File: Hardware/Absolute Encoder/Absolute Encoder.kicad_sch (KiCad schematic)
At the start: 15 parts, among them J1 Conn_01x05, U1 74LS165, U2 74LS165

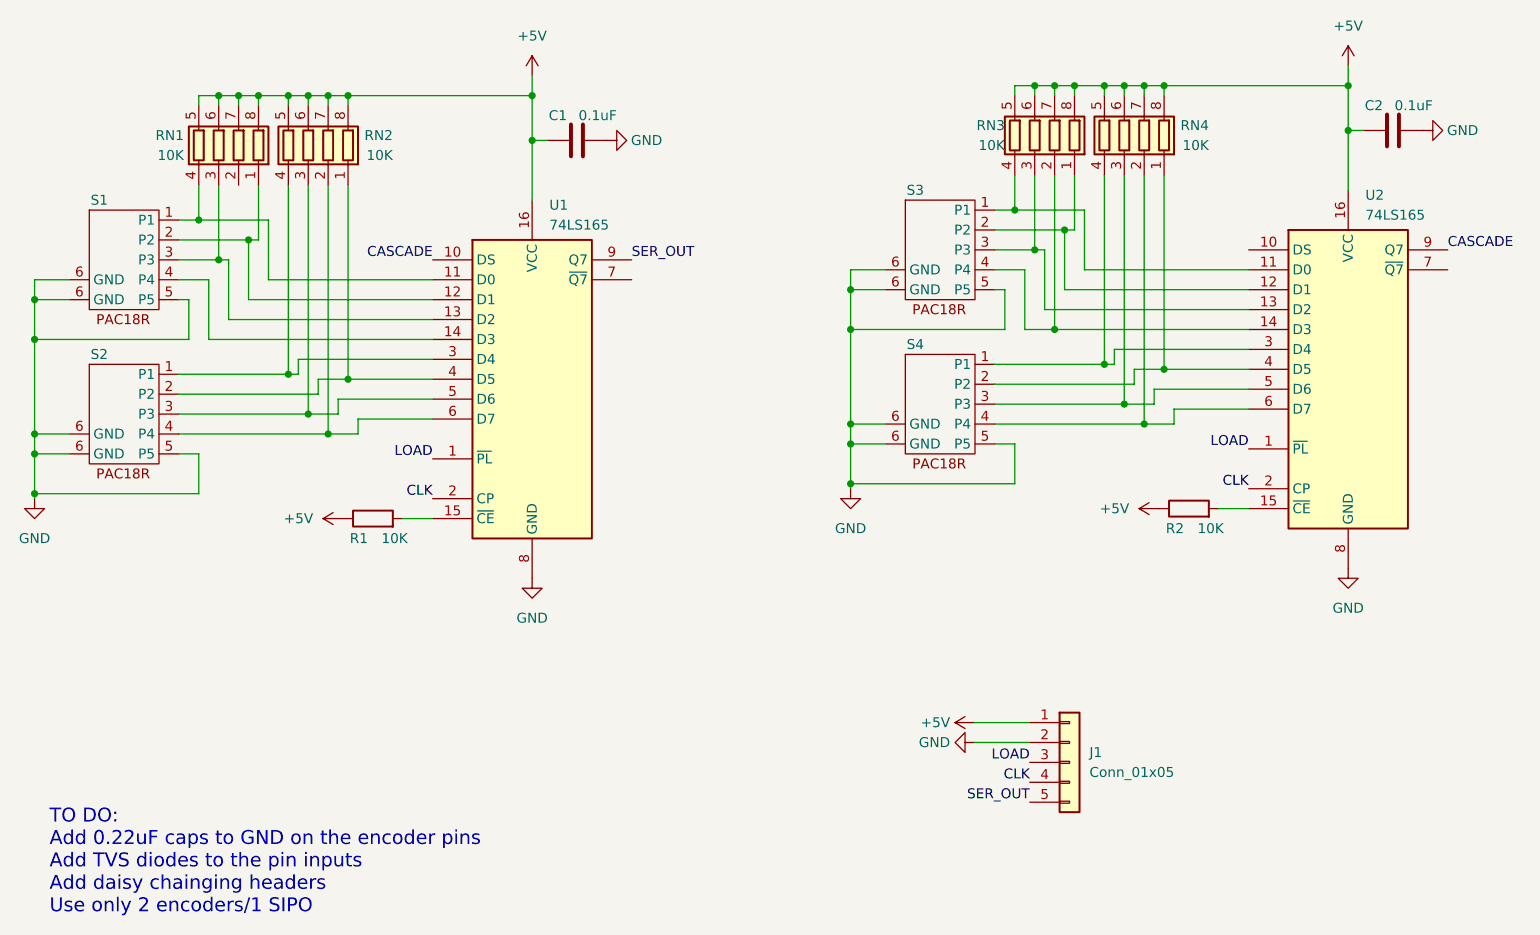
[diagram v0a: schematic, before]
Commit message: Added mount holes
First draft of the silk
Mount Holes
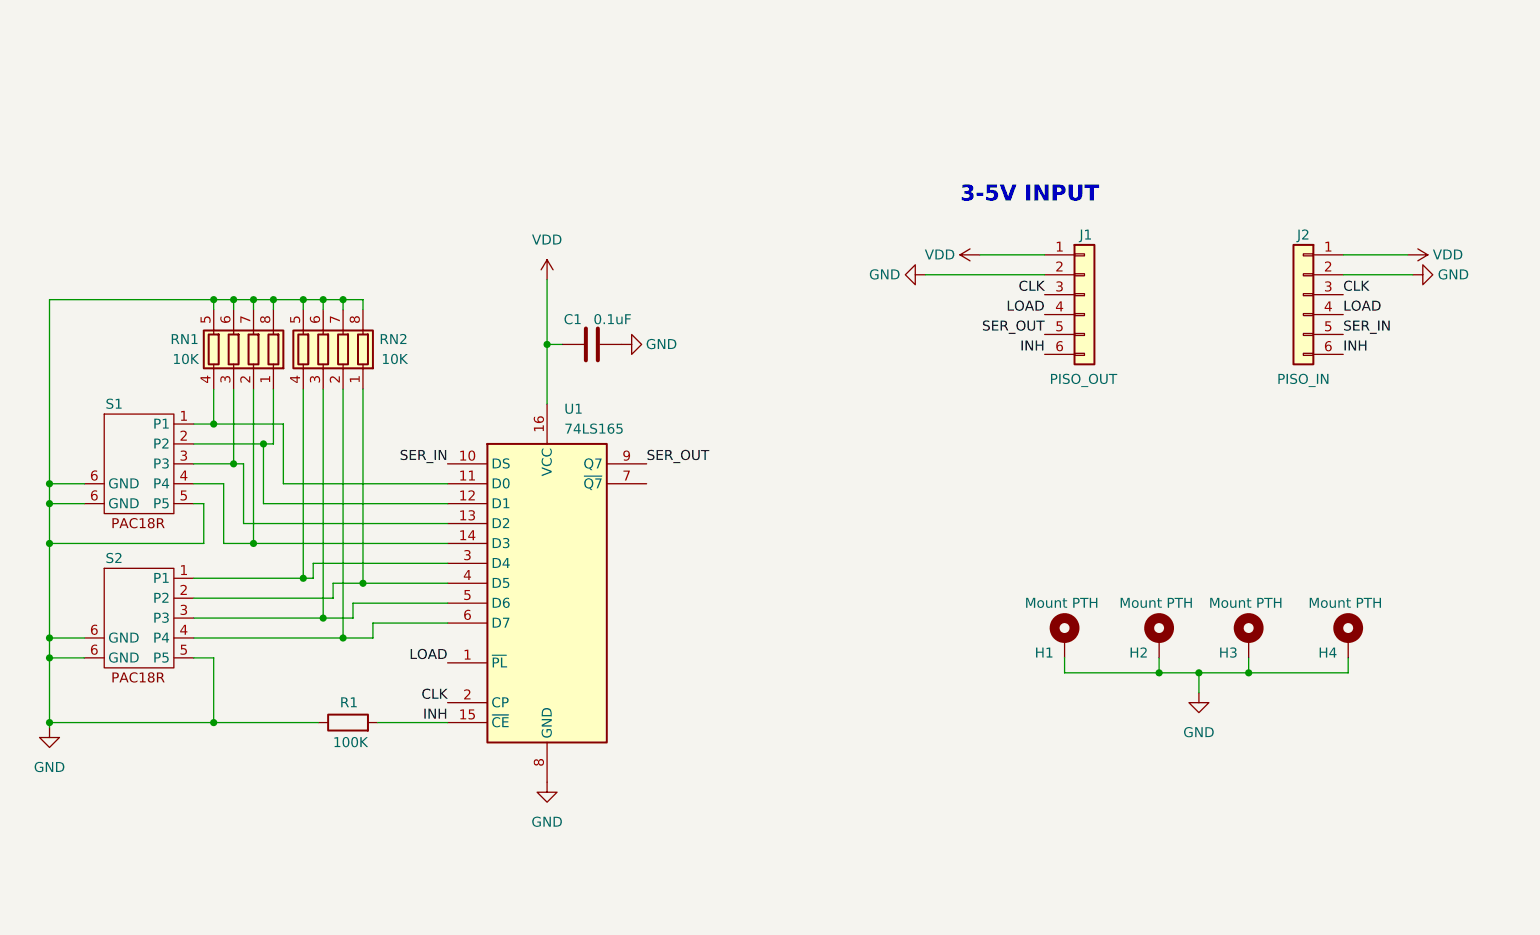
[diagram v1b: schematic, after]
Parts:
- removed C2: 0.1uF, Capacitor_SMD:C_0603_1608Metric, symbol Device:C
- removed R2: 10K, Resistor_SMD:R_0603_1608Metric, symbol Device:R
- removed RN3, RN4: 10K, Resistor_SMD:R_Array_Concave_4x0402, symbol Device:R_Pack04
- removed S3, S4: ~, Flywheel:PAC18R, symbol Flywheel_Library:PAC18R
- removed U2: 74LS165, Package_SO:SOIC-16_3.9x9.9mm_P1.27mm, symbol 74xx:74LS165
- added H1, H2, H3, H4: Mount PTH, MountingHole:MountingHole_2.2mm_M2_Pad_TopBottom, symbol Mechanical:MountingHole_Pad
- added J2: PISO_IN, Connector_PinHeader_2.54mm:PinHeader_1x06_P2.54mm_Vertical, symbol Connector_Generic:Conn_01x06
- J1: value Conn_01x05 -> PISO_OUT; footprint Connector_PinHeader_2.54mm:PinHeader_1x05_P2.54mm_Vertical -> Connector_PinHeader_2.54mm:PinHeader_1x06_P2.54mm_Vertical; symbol Connector_Generic:Conn_01x05 -> Connector_Generic:Conn_01x06
- R1: value 10K -> 100K
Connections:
- net CLK: now also J1.3 (Pin_3), J2.3 (Pin_3); no longer J1.4 (Pin_4)
- net GND: now also R1.1, RN1.5 (R4.2), RN1.6 (R3.2), RN1.7 (R2.2), RN1.8 (R1.2), RN2.5 (R4.2), RN2.6 (R3.2), RN2.7 (R2.2), RN2.8 (R1.2), H1.1, H2.1, H3.1, H4.1, J2.2 (Pin_2)
- net LOAD: now also J1.4 (Pin_4), J2.4 (Pin_4); no longer J1.3 (Pin_3)
- net at S1.4 (P4), U1.14 (D3): now also RN1.2 (R2.1)
- net INH: now reaches R1.2, U1.15 (~{CE})
- net INH: now also J1.6 (Pin_6), J2.6 (Pin_6)
- removed net +5V: C1.1, J1.1 (Pin_1), R1.1, RN1.5 (R4.2), RN1.6 (R3.2), RN1.7 (R2.2), RN1.8 (R1.2), RN2.5 (R4.2), RN2.6 (R3.2), RN2.7 (R2.2), RN2.8 (R1.2), U1.16 (VCC)
- net CASCADE renamed SER_IN
- net SER_IN: now also J2.5 (Pin_5)
- new net VDD: C1.1, J1.1 (Pin_1), J2.1 (Pin_1), U1.16 (VCC)
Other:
- note added: "3-5V INPUT"
- note removed: "TO DO: Add 0.22uF caps to GND on the encoder pins Add TVS diodes to the pin inputs Add daisy chainging headers Use only 2 encoders/1 SIPO"
- moved on the sheet: C1, R1, RN1, RN2, S1, S2, U1
